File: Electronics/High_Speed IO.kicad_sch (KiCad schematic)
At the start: 6 parts, among them J1 HDMI_A, J2 Conn_01x22_Female, U1 RT9742SNGV

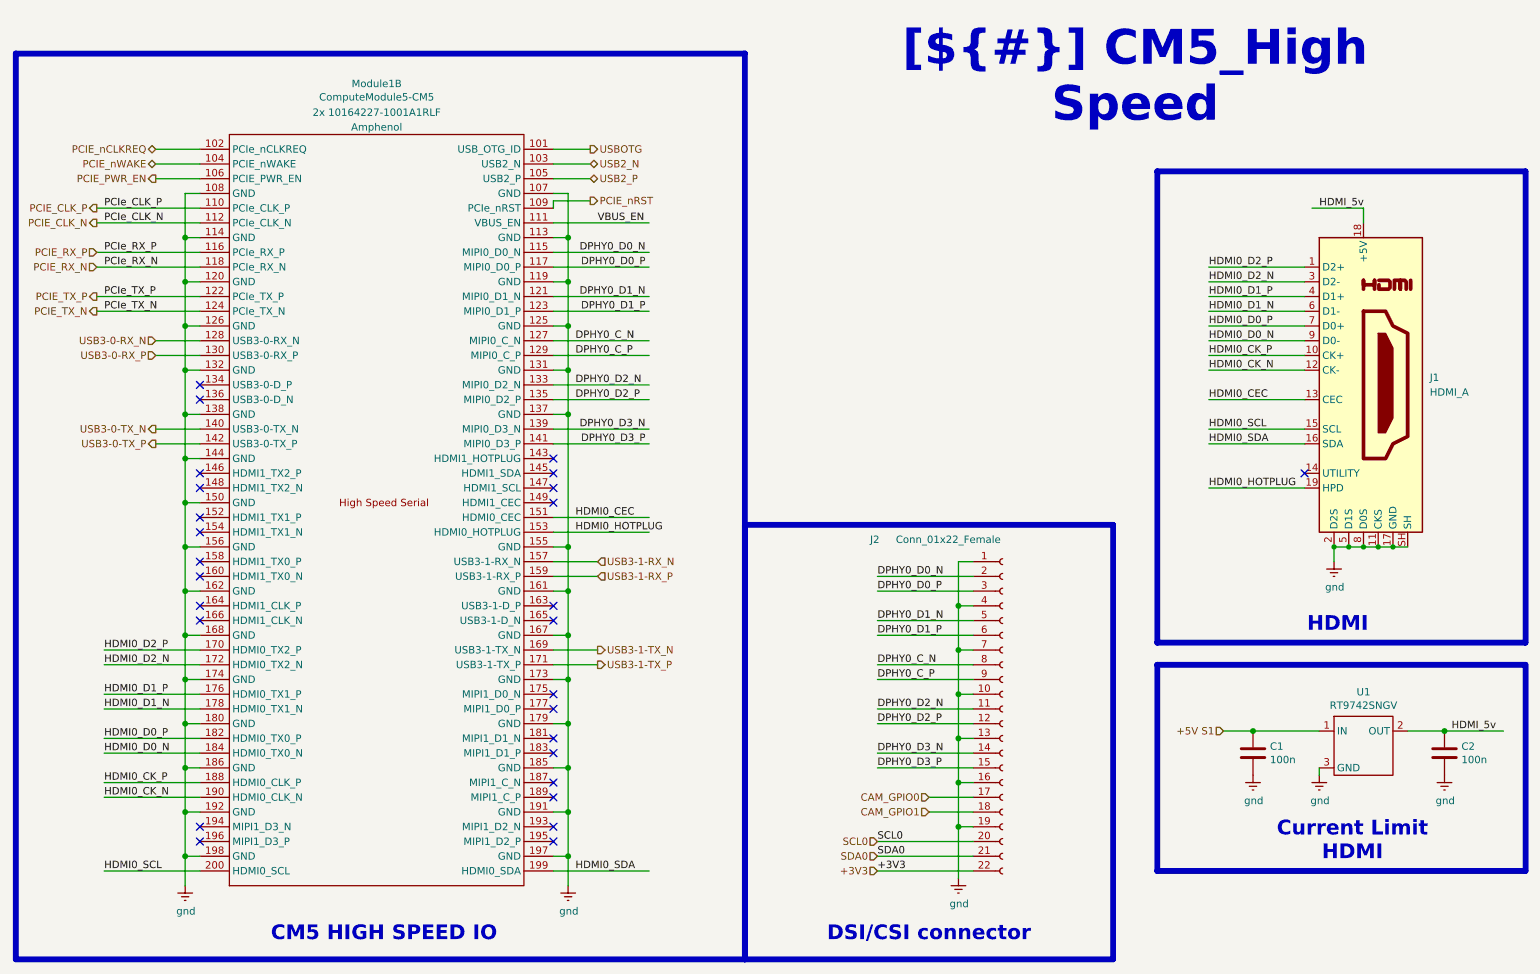
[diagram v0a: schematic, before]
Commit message: Power symbols changed and sata hub fixed schem
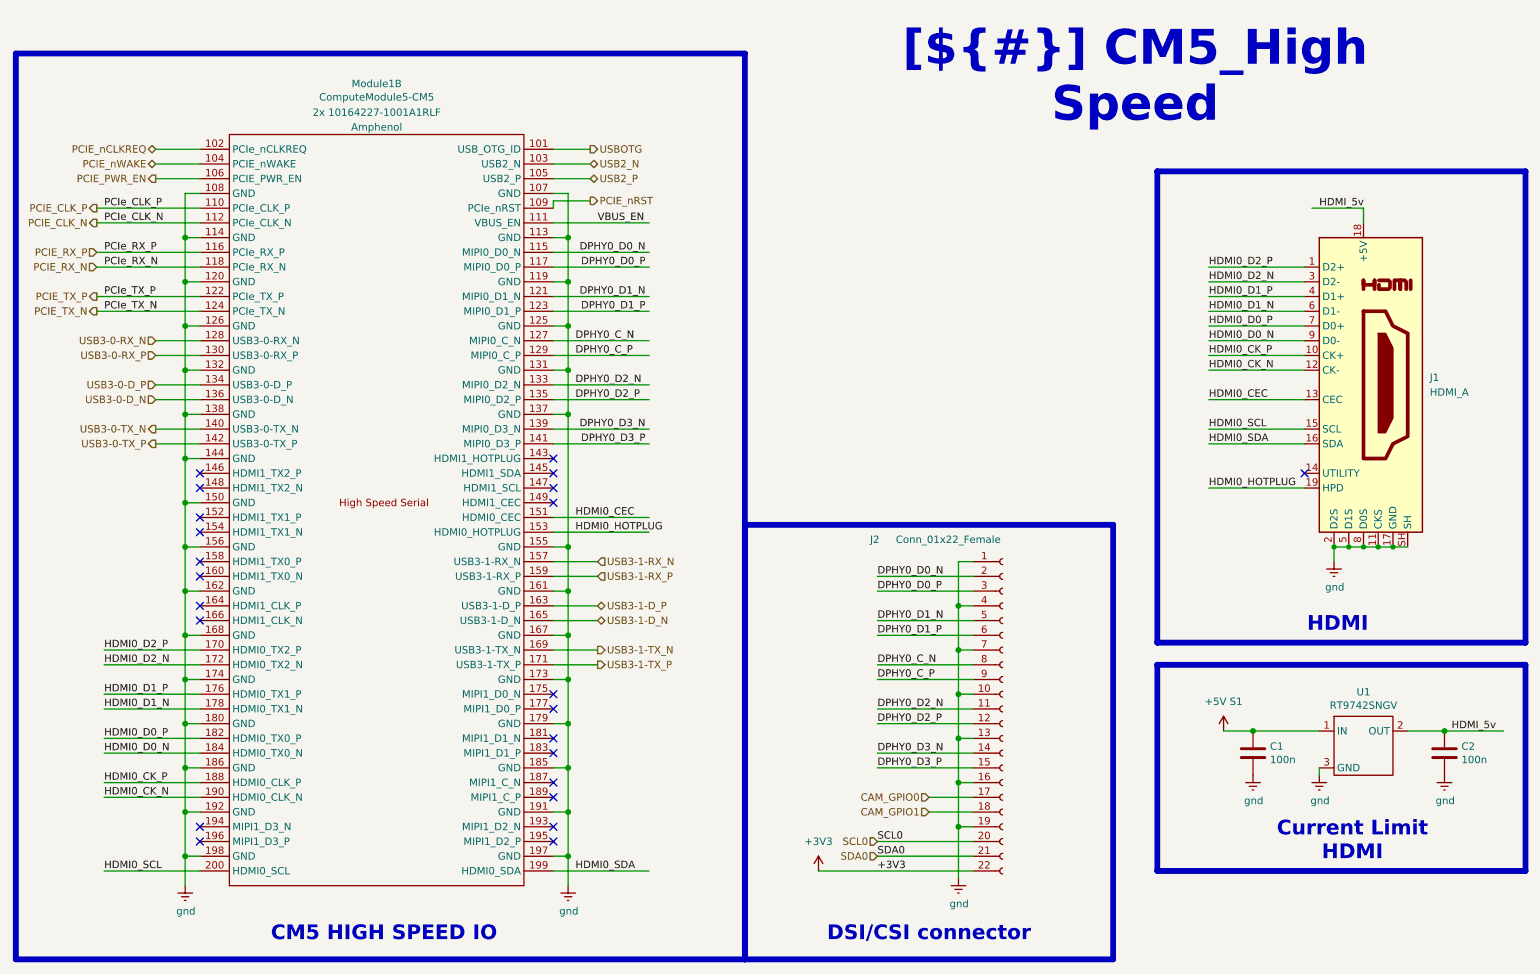
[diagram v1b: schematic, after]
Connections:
- net USB3-0-D_P: now reaches Module1.134 (USB3-0-D_P)
- net USB3-0-D_N: now reaches Module1.136 (USB3-0-D_N)
- net USB3-1-D_P: now reaches Module1.163 (USB3-1-D_P)
- net USB3-1-D_N: now reaches Module1.165 (USB3-1-D_N)
- no-connect marks 27 -> 23
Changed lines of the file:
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@@
 	)
 	(no_connect
-		(at 107.95 114.3)
-	)
-	(no_connect
 		(at 46.99 96.52)
 	)
@@
 	)
 	(no_connect
-		(at 107.95 111.76)
-	)
-	(no_connect
 		(at 107.95 152.4)
 	)
@@
 	)
 	(no_connect
-		(at 46.99 73.66)
-	)
-	(no_connect
 		(at 46.99 91.44)
 	)
 	(no_connect
-		(at 46.99 76.2)
-	)
-	(no_connect
 		(at 46.99 149.86)
 	)
@@
 	(wire
 		(pts
+			(xy 39.37 76.2) (xy 46.99 76.2)
+		)
+		(stroke
+			(width 0)
+			(type default)
+		)
+	)
+	(wire
+		(pts
 			(xy 107.95 124.46) (xy 110.49 124.46)
 		)
@@
 	(wire
 		(pts
-			(xy 240.03 139.7) (xy 240.03 140.97)
+			(xy 39.37 73.66) (xy 46.99 73.66)
 		)
 		(stroke
 			(width 0)
-			(type solid)
+			(type default)
 		)
 	)
 	(wire
 		(pts
-			(xy 107.95 63.5) (xy 110.49 63.5)
+			(xy 240.03 139.7) (xy 240.03 140.97)
 		)
 		(stroke
@@
 	(wire
 		(pts
-			(xy 44.45 132.08) (xy 46.99 132.08)
+			(xy 107.95 63.5) (xy 110.49 63.5)
 		)
 		(stroke
@@
 	(wire
 		(pts
-			(xy 107.95 104.14) (xy 115.57 104.14)
+			(xy 44.45 132.08) (xy 46.99 132.08)
 		)
 		(stroke
@@
 	(wire
 		(pts
-			(xy 107.95 66.04) (xy 124.46 66.04)
+			(xy 107.95 104.14) (xy 115.57 104.14)
 		)
 		(stroke
@@
 	(wire
 		(pts
-			(xy 107.95 121.92) (xy 115.57 121.92)
+			(xy 107.95 66.04) (xy 124.46 66.04)
 		)
 		(stroke
@@
 	(wire
 		(pts
-			(xy 110.49 109.22) (xy 110.49 116.84)
+			(xy 107.95 121.92) (xy 115.57 121.92)
 		)
 		(stroke
@@
 	(wire
 		(pts
-			(xy 180.34 157.48) (xy 163.83 157.48)
+			(xy 110.49 109.22) (xy 110.49 116.84)
 		)
 		(stroke
@@
 	(wire
 		(pts
+			(xy 115.57 114.3) (xy 107.95 114.3)
+		)
+		(stroke
+			(width 0)
+			(type default)
+		)
+	)
+	(wire
+		(pts
 			(xy 44.45 63.5) (xy 46.99 63.5)
 		)
@@
 	(wire
 		(pts
+			(xy 153.67 157.48) (xy 180.34 157.48)
+		)
+		(stroke
+			(width 0)
+			(type default)
+		)
+	)
+	(wire
+		(pts
+			(xy 115.57 111.76) (xy 107.95 111.76)
+		)
+		(stroke
+			(width 0)
+			(type default)
+		)
+	)
+	(wire
+		(pts
 			(xy 29.21 43.18) (xy 46.99 43.18)
 		)
@@
 		)
 	)
-	(hierarchical_label "USB3-1-TX_N"
-		(shape output)
-		(at 115.57 119.38 0)
+	(hierarchical_label "USB3-1-D_P"
+		(shape bidirectional)
+		(at 115.57 111.76 0)
 		(effects
 			(font
@@
 		)
 	)
-	(hierarchical_label "PCIE_nRST"
+	(hierarchical_label "USB3-1-TX_N"
 		(shape output)
-		(at 114.3 41.91 0)
+		(at 115.57 119.38 0)
 		(effects
 			(font
@@
 		)
 	)
-	(hierarchical_label "+3V3"
-		(shape input)
-		(at 163.83 157.48 180)
+	(hierarchical_label "PCIE_nRST"
+		(shape output)
+		(at 114.3 41.91 0)
 		(effects
 			(font
 				(size 1.27 1.27)
 			)
-			(justify right)
+			(justify left)
 		)
 	)
@@
 		)
 	)
-	(hierarchical_label "+5V S1"
-		(shape input)
-		(at 223.52 133.35 180)
-		(effects
-			(font
-				(size 1.27 1.27)
-			)
-			(justify right)
-		)
-	)
 	(hierarchical_label "PCIE_nWAKE"
 		(shape bidirectional)
@@
 		)
 	)
+	(hierarchical_label "USB3-1-D_N"
+		(shape bidirectional)
+		(at 115.57 114.3 0)
+		(effects
+			(font
+				(size 1.27 1.27)
+			)
+			(justify left)
+		)
+	)
 	(hierarchical_label "PCIE_nCLKREQ"
 		(shape bidirectional)
@@
 		)
 	)
+	(hierarchical_label "USB3-0-D_P"
+		(shape input)
+		(at 39.37 73.66 180)
+		(effects
+			(font
+				(size 1.27 1.27)
+			)
+			(justify right)
+		)
+	)
+	(hierarchical_label "USB3-0-D_N"
+		(shape input)
+		(at 39.37 76.2 180)
+		(effects
+			(font
+				(size 1.27 1.27)
+			)
+			(justify right)
+		)
+	)
 	(hierarchical_label "USB3-0-RX_N"
 		(shape input)
@@
 		(polyline
 			(pts
-				(xy 114.3 102.87) (xy 114.3 123.19) (xy 111.76 123.19) (xy 111.76 102.87)
+				(xy 114.3 102.87) (xy 114.3 124.46) (xy 111.76 124.46) (xy 111.76 102.87)
 			)
 			(stroke
@@
 		(polyline
 			(pts
-				(xy 124.46 34.29) (xy 124.46 39.37) (xy 109.22 39.37) (xy 109.22 34.29)
+				(xy 43.18 40.64) (xy 43.18 63.5) (xy 40.64 63.5) (xy 40.64 40.64)
 			)
 			(stroke
@@
 		(polyline
 			(pts
-				(xy 43.18 64.77) (xy 43.18 85.09) (xy 40.64 85.09) (xy 40.64 64.77)
+				(xy 43.18 64.77) (xy 43.18 86.36) (xy 40.64 86.36) (xy 40.64 64.77)
 			)
 			(stroke
@@
 		(polyline
 			(pts
-				(xy 43.18 40.64) (xy 43.18 63.5) (xy 40.64 63.5) (xy 40.64 40.64)
+				(xy 124.46 34.29) (xy 124.46 39.37) (xy 109.22 39.37) (xy 109.22 34.29)
 			)
 			(stroke
@@
 		(length 2.54)
 		(shape round)
-		(at 40.64 74.93 90)
+		(at 40.64 86.36 90)
 		(effects
 			(font
@@
 		)
 		(property "Netclass" "USB DIF"
-			(at 29.464 74.93 0)
+			(at 29.464 86.36 0)
 			(effects
 				(font
@@
 		)
 		(property "Component Class" ""
-			(at -127 10.16 0)
+			(at -127 21.59 0)
 			(effects
 				(font
@@
 		(length 2.54)
 		(shape round)
-		(at 114.3 113.03 270)
+		(at 114.3 124.46 270)
 		(effects
 			(font
@@
 		)
 		(property "Netclass" "USB DIF"
-			(at 117.602 113.03 0)
+			(at 117.348 124.46 0)
 			(effects
 				(font
@@
 		)
 		(property "Component Class" ""
-			(at -45.72 60.96 0)
+			(at -45.72 72.39 0)
 			(effects
 				(font
@@
 		(length 2.54)
 		(shape round)
-		(at 228.6 133.35 0)
-		(effects
-			(font
-				(size 1.27 1.27)
-			)
-			(justify left bottom)
-		)
-		(property "Netclass" "PWR RAIL"
-			(at 228.092 129.286 0)
-			(effects
-				(font
-					(size 1.27 1.27)
-				)
-				(justify left)
-			)
-		)
-		(property "Component Class" ""
-			(at 107.95 12.7 0)
-			(effects
-				(font
-					(size 1.27 1.27)
-					(italic yes)
-				)
-			)
-		)
-	)
-	(netclass_flag ""
-		(length 2.54)
-		(shape round)
 		(at 256.54 133.35 0)
 		(effects
@@
 	)
 	(symbol
+		(lib_id "power:+5V")
+		(at 223.52 133.35 0)
+		(unit 1)
+		(exclude_from_sim no)
+		(in_bom yes)
+		(on_board yes)
+		(dnp no)
+		(fields_autoplaced yes)
+		(property "Reference" "#PWR0182"
+			(at 223.52 137.16 0)
+			(effects
+				(font
+					(size 1.27 1.27)
+				)
+				(hide yes)
+			)
+		)
+		(property "Value" "+5V S1"
+			(at 223.52 128.27 0)
+			(effects
+				(font
+					(size 1.27 1.27)
+				)
+			)
+		)
+		(property "Footprint" ""
+			(at 223.52 133.35 0)
+			(effects
+				(font
+					(size 1.27 1.27)
+				)
+				(hide yes)
+			)
+		)
+		(property "Datasheet" ""
+			(at 223.52 133.35 0)
+			(effects
+				(font
+					(size 1.27 1.27)
+				)
+				(hide yes)
+			)
+		)
+		(property "Description" "Power symbol creates a global label with name \"+5V\""
+			(at 223.52 133.35 0)
+			(effects
+				(font
+					(size 1.27 1.27)
+				)
+				(hide yes)
+			)
+		)
+		(pin "1"
+		)
+		(instances
+			(project "CM5 Nas"
+				(path "/0650c7a8-acba-429c-9f8e-eec0baf0bc1c/fede4c36-00cc-4d3d-b71c-5243ba232202/7d5a1283-086b-46b0-8df7-a9850521fb5e"
+					(reference "#PWR0182")
+					(unit 1)
+				)
+			)
+		)
+	)
+	(symbol
 		(lib_id "Connector:HDMI_A")
 		(at 247.65 73.66 0)
@@
 		)
 		(instances
-			(project ""
+			(project "CM5 Nas"
 				(path "/0650c7a8-acba-429c-9f8e-eec0baf0bc1c/fede4c36-00cc-4d3d-b71c-5243ba232202/7d5a1283-086b-46b0-8df7-a9850521fb5e"
 					(reference "J1")
 					(unit 1)
 				)
+			)
+		)
+	)
+	(symbol
+		(lib_id "power:+3V3")
+		(at 153.67 157.48 0)
+		(unit 1)
+		(exclude_from_sim no)
+		(in_bom yes)
+		(on_board yes)
+		(dnp no)
+		(fields_autoplaced yes)
+		(property "Reference" "#PWR0181"
+			(at 153.67 161.29 0)
+			(effects
+				(font
+					(size 1.27 1.27)
+				)
+				(hide yes)
+			)
+		)
+		(property "Value" "+3V3"
+			(at 153.67 152.4 0)
+			(effects
+				(font
+					(size 1.27 1.27)
+				)
+			)
+		)
+		(property "Footprint" ""
+			(at 153.67 157.48 0)
+			(effects
+				(font
+					(size 1.27 1.27)
+				)
+				(hide yes)
+			)
+		)
+		(property "Datasheet" ""
+			(at 153.67 157.48 0)
+			(effects
+				(font
+					(size 1.27 1.27)
+				)
+				(hide yes)
+			)
+		)
+		(property "Description" "Power symbol creates a global label with name \"+3V3\""
+			(at 153.67 157.48 0)
+			(effects
+				(font
+					(size 1.27 1.27)
+				)
+				(hide yes)
+			)
+		)
+		(pin "1"
+		)
+		(instances
+			(project "CM5 Nas"
+				(path "/0650c7a8-acba-429c-9f8e-eec0baf0bc1c/fede4c36-00cc-4d3d-b71c-5243ba232202/7d5a1283-086b-46b0-8df7-a9850521fb5e"
+					(reference "#PWR0181")
+					(unit 1)
+				)
